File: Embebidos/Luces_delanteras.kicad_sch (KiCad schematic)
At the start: 10 parts, among them J3 RJ45, J4 RJ45

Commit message: anotaciones_fix
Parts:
- gave numbers to parts that had none: 4
- renumbered J4 to J6, J3 to J7, R1a to R1a1, R2a to R2a1, R3a to R3a1, R4a to R4a1
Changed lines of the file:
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@@
   (symbol (lib_id "Connector:RJ45") (at 97.79 86.36 180) (unit 1)
     (in_bom yes) (on_board yes)
-    (property "Reference" "J4" (id 0) (at 106.172 86.4616 0)
+    (property "Reference" "J6" (id 0) (at 106.172 86.4616 0)
       (effects (font (size 1.27 1.27)) (justify right))
     )
@@
   (symbol (lib_id "Connector:RJ45") (at 167.64 93.98 0) (unit 1)
     (in_bom yes) (on_board yes)
-    (property "Reference" "J3" (id 0) (at 169.0878 77.0382 0))
+    (property "Reference" "J7" (id 0) (at 169.0878 77.0382 0))
     (property "Value" "RJ45" (id 1) (at 169.0878 79.3496 0))
     (property "Footprint" "" (id 2) (at 167.64 93.345 90)
@@
   (symbol (lib_id "Device:R") (at 185.42 99.06 90) (unit 1)
     (in_bom yes) (on_board yes) (fields_autoplaced)
-    (property "Reference" "R1a" (id 0) (at 185.42 92.71 90))
+    (property "Reference" "R1a1" (id 0) (at 185.42 92.71 90))
     (property "Value" "1K" (id 1) (at 185.42 95.25 90))
     (property "Footprint" "" (id 2) (at 185.42 100.838 90)
@@
   (symbol (lib_id "power:+5V") (at 189.23 120.65 180) (unit 1)
     (in_bom yes) (on_board yes) (fields_autoplaced)
-    (property "Reference" "#PWR?" (id 0) (at 189.23 116.84 0)
+    (property "Reference" "#PWR035" (id 0) (at 189.23 116.84 0)
       (effects (font (size 1.27 1.27)) hide)
     )
@@
   (symbol (lib_id "Device:R") (at 55.88 111.76 0) (unit 1)
     (in_bom yes) (on_board yes) (fields_autoplaced)
-    (property "Reference" "R4a" (id 0) (at 58.42 110.4899 0)
+    (property "Reference" "R4a1" (id 0) (at 58.42 110.4899 0)
       (effects (font (size 1.27 1.27)) (justify left))
     )
@@
   (symbol (lib_id "Connector:Conn_01x08_Female") (at 41.91 69.85 180) (unit 1)
     (in_bom yes) (on_board yes) (fields_autoplaced)
-    (property "Reference" "J?" (id 0) (at 42.545 54.61 0))
+    (property "Reference" "J5" (id 0) (at 42.545 54.61 0))
     (property "Value" "Joystick" (id 1) (at 42.545 57.15 0))
     (property "Footprint" "" (id 2) (at 41.91 69.85 0)
@@
   (symbol (lib_id "Device:Q_PMOS_DSG") (at 228.6 114.3 0) (unit 1)
     (in_bom yes) (on_board yes) (fields_autoplaced)
-    (property "Reference" "Q?" (id 0) (at 234.95 113.0299 0)
+    (property "Reference" "Q3" (id 0) (at 234.95 113.0299 0)
       (effects (font (size 1.27 1.27)) (justify left))
     )
@@
   (symbol (lib_id "Connector:Conn_01x04_Female") (at 38.1 102.87 180) (unit 1)
     (in_bom yes) (on_board yes) (fields_autoplaced)
-    (property "Reference" "J?" (id 0) (at 38.735 92.71 0))
+    (property "Reference" "J3" (id 0) (at 38.735 92.71 0))
     (property "Value" "Pantallas I2C" (id 1) (at 38.735 95.25 0))
     (property "Footprint" "" (id 2) (at 38.1 102.87 0)
@@
   (symbol (lib_id "Connector:Conn_01x03_Female") (at 38.1 120.65 180) (unit 1)
     (in_bom yes) (on_board yes) (fields_autoplaced)
-    (property "Reference" "J?" (id 0) (at 38.735 113.03 0))
+    (property "Reference" "J4" (id 0) (at 38.735 113.03 0))
     (property "Value" "Luz_delantera" (id 1) (at 38.735 115.57 0))
     (property "Footprint" "" (id 2) (at 38.1 120.65 0)
@@
   (symbol (lib_id "power:GND") (at 182.88 66.04 180) (unit 1)
     (in_bom yes) (on_board yes) (fields_autoplaced)
-    (property "Reference" "#PWR?" (id 0) (at 182.88 59.69 0)
+    (property "Reference" "#PWR034" (id 0) (at 182.88 59.69 0)
       (effects (font (size 1.27 1.27)) hide)
     )
@@
   (symbol (lib_id "power:+5V") (at 231.14 121.92 180) (unit 1)
     (in_bom yes) (on_board yes) (fields_autoplaced)
-    (property "Reference" "#PWR?" (id 0) (at 231.14 118.11 0)
+    (property "Reference" "#PWR036" (id 0) (at 231.14 118.11 0)
       (effects (font (size 1.27 1.27)) hide)
     )
@@
   (symbol (lib_id "Device:R") (at 193.04 96.52 90) (unit 1)
     (in_bom yes) (on_board yes) (fields_autoplaced)
-    (property "Reference" "R2a" (id 0) (at 193.04 90.17 90))
+    (property "Reference" "R2a1" (id 0) (at 193.04 90.17 90))
     (property "Value" "1K" (id 1) (at 193.04 92.71 90))
     (property "Footprint" "" (id 2) (at 193.04 98.298 90)
@@
   (symbol (lib_id "Device:R") (at 200.66 93.98 90) (unit 1)
     (in_bom yes) (on_board yes) (fields_autoplaced)
-    (property "Reference" "R3a" (id 0) (at 200.66 87.63 90))
+    (property "Reference" "R3a1" (id 0) (at 200.66 87.63 90))
     (property "Value" "1K" (id 1) (at 200.66 90.17 90))
     (property "Footprint" "" (id 2) (at 200.66 95.758 90)

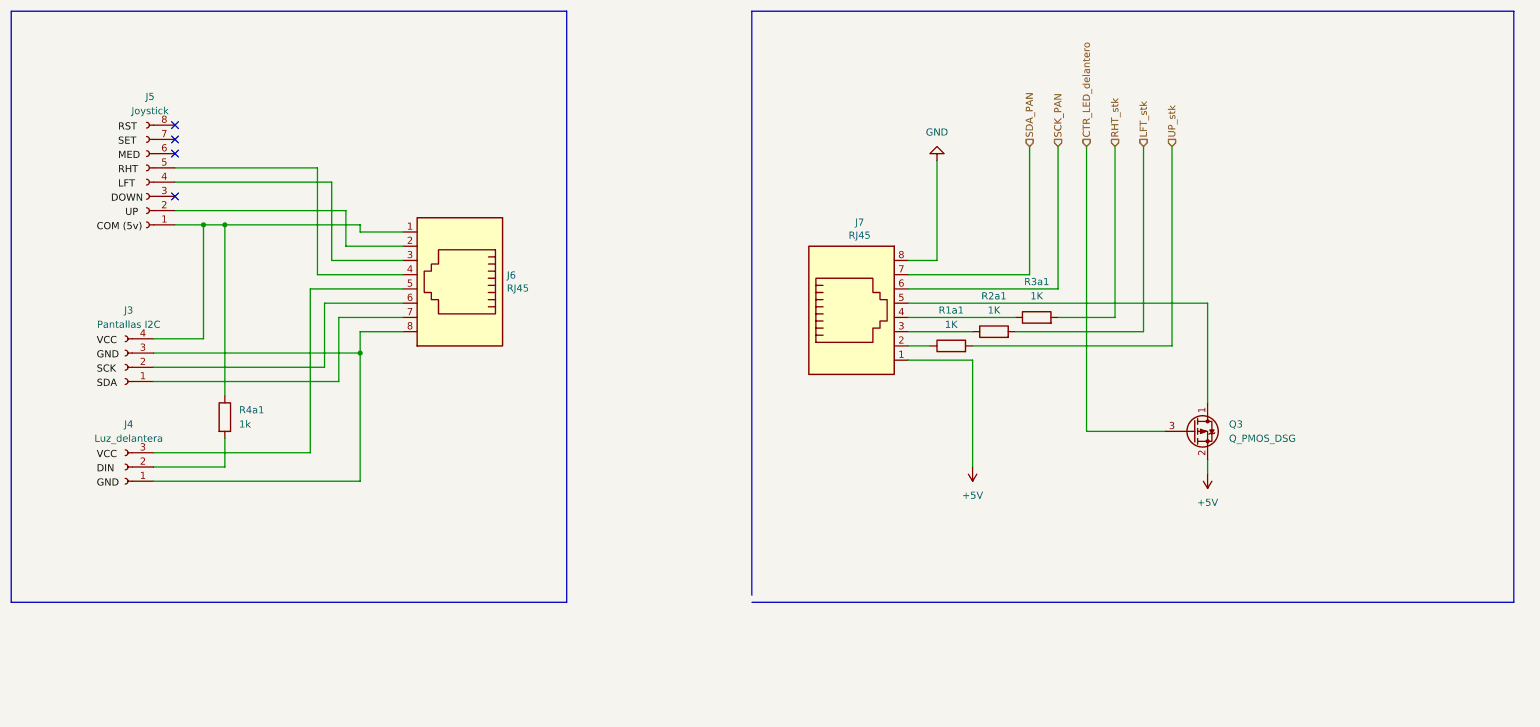
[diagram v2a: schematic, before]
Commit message: Cambio de anotacion y Vcc ldr
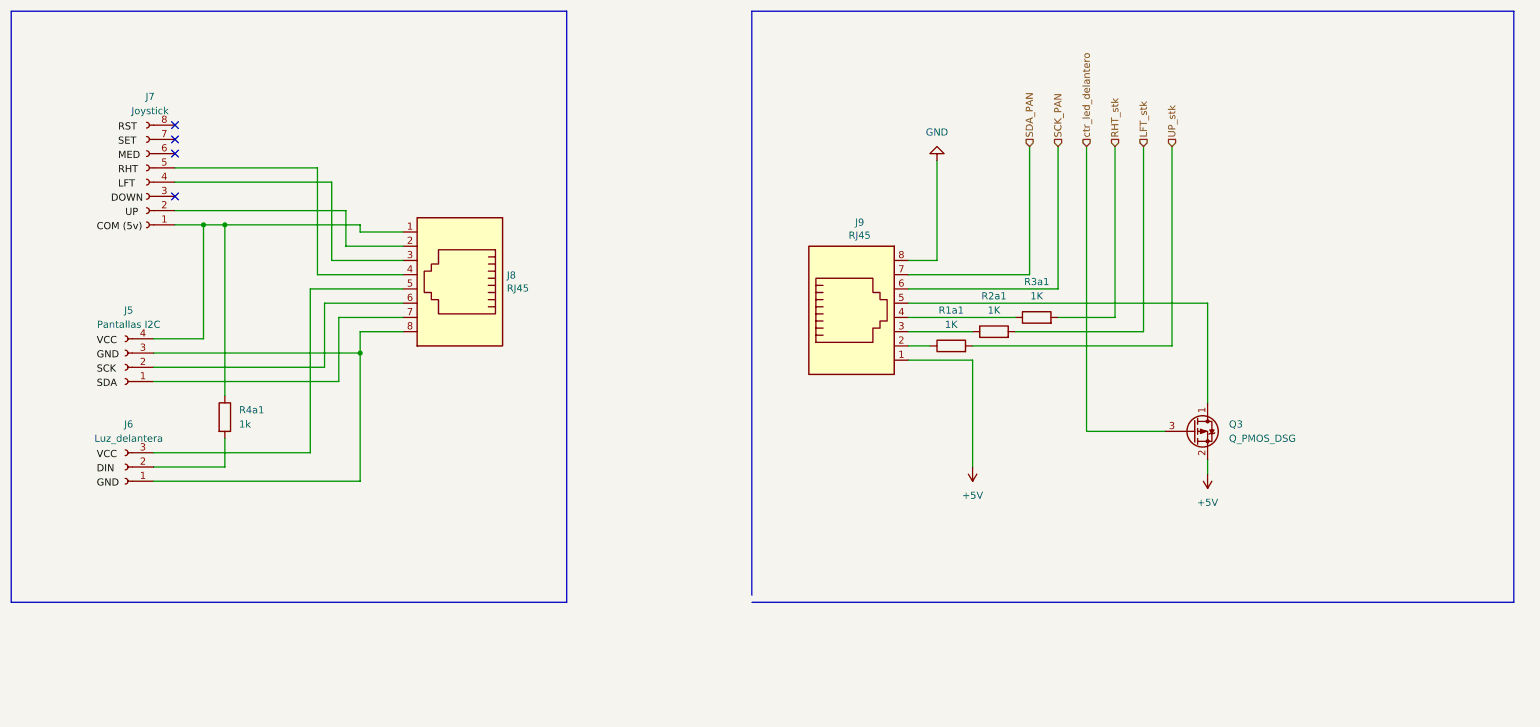
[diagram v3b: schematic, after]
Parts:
- renumbered J3 to J5, J4 to J6, J5 to J7, J6 to J8, J7 to J9
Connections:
- net CTR_LED_delantero renamed ctr_led_delantero
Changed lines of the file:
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@@
     (effects (font (size 1.27 1.27)) (justify left))
   )
-  (hierarchical_label "CTR_LED_delantero" (shape input) (at 209.55 63.5 90)
+  (hierarchical_label "ctr_led_delantero" (shape input) (at 209.55 63.5 90)
     (effects (font (size 1.27 1.27)) (justify left))
   )
@@
   (symbol (lib_id "Connector:RJ45") (at 97.79 86.36 180) (unit 1)
     (in_bom yes) (on_board yes)
-    (property "Reference" "J6" (id 0) (at 106.172 86.4616 0)
+    (property "Reference" "J8" (id 0) (at 106.172 86.4616 0)
       (effects (font (size 1.27 1.27)) (justify right))
     )
@@
   (symbol (lib_id "Connector:RJ45") (at 167.64 93.98 0) (unit 1)
     (in_bom yes) (on_board yes)
-    (property "Reference" "J7" (id 0) (at 169.0878 77.0382 0))
+    (property "Reference" "J9" (id 0) (at 169.0878 77.0382 0))
     (property "Value" "RJ45" (id 1) (at 169.0878 79.3496 0))
     (property "Footprint" "" (id 2) (at 167.64 93.345 90)
@@
   (symbol (lib_id "power:+5V") (at 189.23 120.65 180) (unit 1)
     (in_bom yes) (on_board yes) (fields_autoplaced)
-    (property "Reference" "#PWR035" (id 0) (at 189.23 116.84 0)
+    (property "Reference" "#PWR036" (id 0) (at 189.23 116.84 0)
       (effects (font (size 1.27 1.27)) hide)
     )
@@
   (symbol (lib_id "Connector:Conn_01x08_Female") (at 41.91 69.85 180) (unit 1)
     (in_bom yes) (on_board yes) (fields_autoplaced)
-    (property "Reference" "J5" (id 0) (at 42.545 54.61 0))
+    (property "Reference" "J7" (id 0) (at 42.545 54.61 0))
     (property "Value" "Joystick" (id 1) (at 42.545 57.15 0))
     (property "Footprint" "" (id 2) (at 41.91 69.85 0)
@@
   (symbol (lib_id "Connector:Conn_01x04_Female") (at 38.1 102.87 180) (unit 1)
     (in_bom yes) (on_board yes) (fields_autoplaced)
-    (property "Reference" "J3" (id 0) (at 38.735 92.71 0))
+    (property "Reference" "J5" (id 0) (at 38.735 92.71 0))
     (property "Value" "Pantallas I2C" (id 1) (at 38.735 95.25 0))
     (property "Footprint" "" (id 2) (at 38.1 102.87 0)
@@
   (symbol (lib_id "Connector:Conn_01x03_Female") (at 38.1 120.65 180) (unit 1)
     (in_bom yes) (on_board yes) (fields_autoplaced)
-    (property "Reference" "J4" (id 0) (at 38.735 113.03 0))
+    (property "Reference" "J6" (id 0) (at 38.735 113.03 0))
     (property "Value" "Luz_delantera" (id 1) (at 38.735 115.57 0))
     (property "Footprint" "" (id 2) (at 38.1 120.65 0)
@@
   (symbol (lib_id "power:GND") (at 182.88 66.04 180) (unit 1)
     (in_bom yes) (on_board yes) (fields_autoplaced)
-    (property "Reference" "#PWR034" (id 0) (at 182.88 59.69 0)
+    (property "Reference" "#PWR035" (id 0) (at 182.88 59.69 0)
       (effects (font (size 1.27 1.27)) hide)
     )
@@
   (symbol (lib_id "power:+5V") (at 231.14 121.92 180) (unit 1)
     (in_bom yes) (on_board yes) (fields_autoplaced)
-    (property "Reference" "#PWR036" (id 0) (at 231.14 118.11 0)
+    (property "Reference" "#PWR037" (id 0) (at 231.14 118.11 0)
       (effects (font (size 1.27 1.27)) hide)
     )

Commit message: Cambios varios
-Conectores movidos a nueva hoja jerarquica

-Transistores DMP colocados en lices delanteras

-Jumpers ubicados para el uso del pin IO13 para SIM800 y LEDHW

-Etiqueta de "no conectado" ubicada en USB_UART
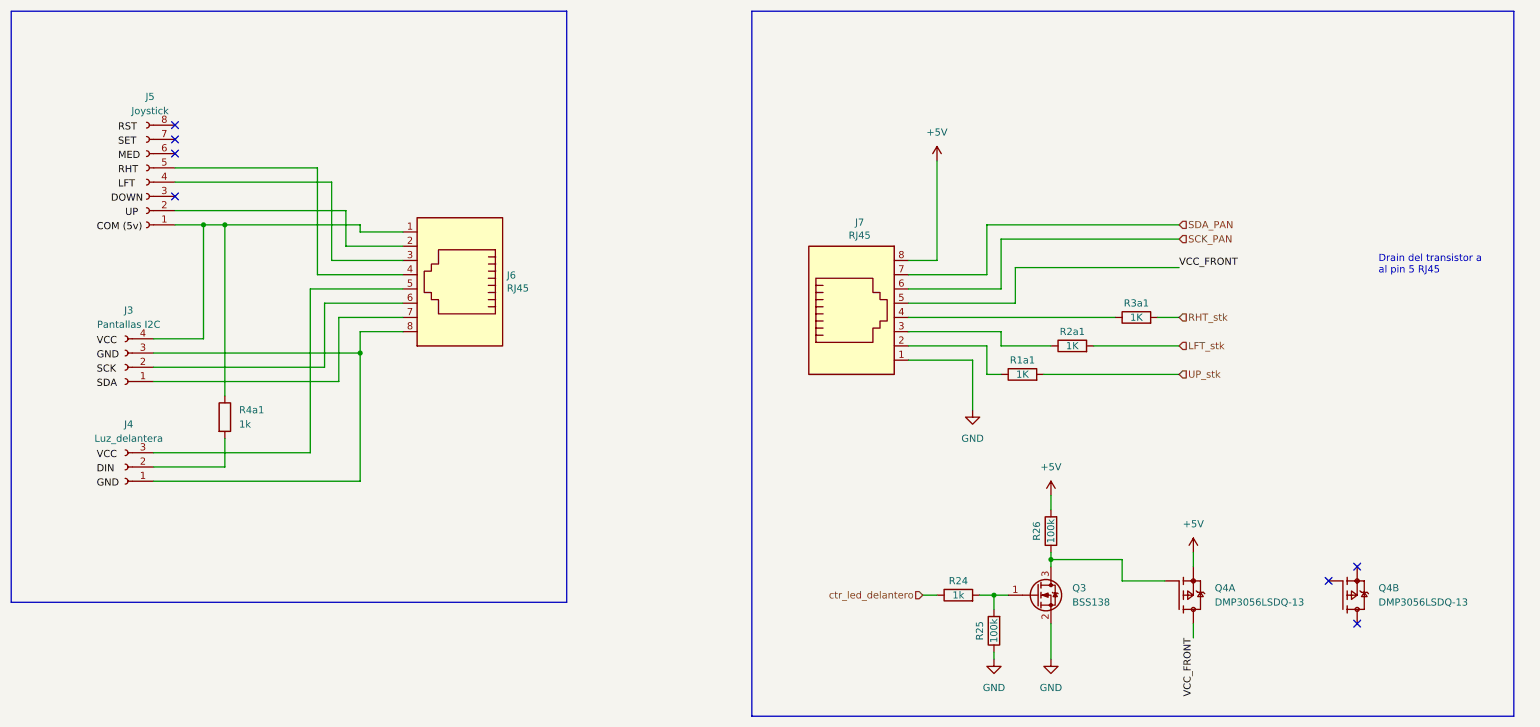
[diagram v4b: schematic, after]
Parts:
- removed Q3: Q_PMOS_DSG, symbol Device:Q_PMOS_DSG
- added Q3: BSS138, Package_TO_SOT_SMD:SOT-23, symbol Transistor_FET:BSS138
- added Q4: DMP3056LSDQ-13, DMP3056LSD:SOIC127P600X175-8N, symbol DMP3056LSDQ-13:DMP3056LSDQ-13
- added R24: 1k, symbol Device:R
- added R25, R26: 100k, symbol Device:R
- renumbered J5 to J3, J6 to J4, J7 to J5, J8 to J6, J9 to J7
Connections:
- net +5V: now also J7.8, Q4.1, R26.2; no longer J7.1
- net GND: now also J7.1, Q3.2 (S), R25.1; no longer J7.8
- net ctr_led_delantero: now also R24.1
- net VCC_FRONT: now reaches J7.5
- net VCC_FRONT: now also Q4.7, Q4.8
- new net: Q3.1 (G), R24.2, R25.2
- new net: Q3.3 (D), Q4.2, R26.1
- new net: Q4.5, Q4.6
- no-connect marks 4 -> 7
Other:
- note added: "Drain del transistor a al pin 5 RJ45"
- moved on the sheet: R1a1, R2a1, R3a1
